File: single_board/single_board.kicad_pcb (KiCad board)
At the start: 4 copper layers, 100 x 100 mm, 121 parts, among them J11 SPI Debug, J17 BOOTSEL, J18 Power, J2 USB_C_Receptacle_USB2.0_16P, J3 SWD, J30 JST_GH_H, J31 JST_GH_H, J33 JST_GH_H, J34 PB_Vertical, J35 JST_GH_H, J36 JST_GH_H, J37 JST_GH_H, J38 PB_Vertical, J39 PB_Vertical, J40 PB_Vertical, J41 PB_Vertical, J42 PB_Vertical, J43 PB_Vertical, J44 PB_Vertical, J45 PB_Vertical, J46 PB_Vertical, J47 PB_Vertical, J48 PB_Vertical, J49 PB_Vertical, J5 JST-GH, J50 PB_Vertical, J53 PB_Vertical, Q1 AO3400A, Q3 AO3401A, SW1 Button, U1 AP2112K-3.3, U3 USBLC6-2SC6, U4 LSM6DSV, U5 STM32G474VBTx, Y2 ABM8-16MHz

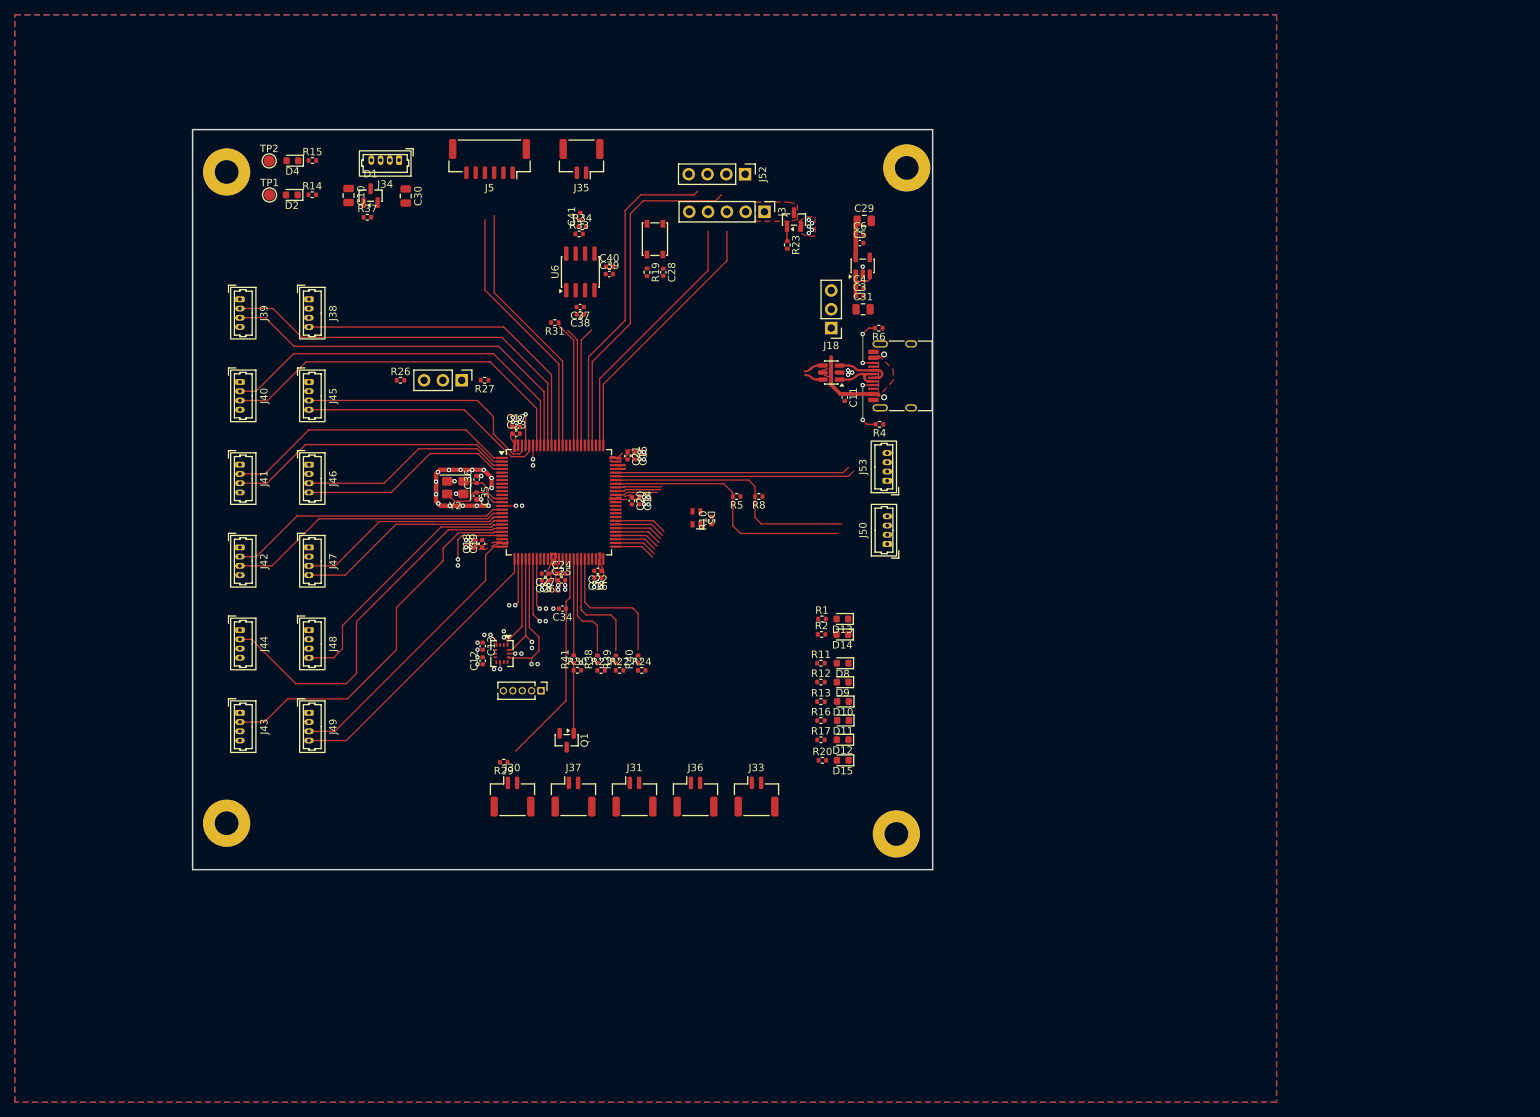
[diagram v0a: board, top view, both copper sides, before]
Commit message: Silkscreen on LEDs
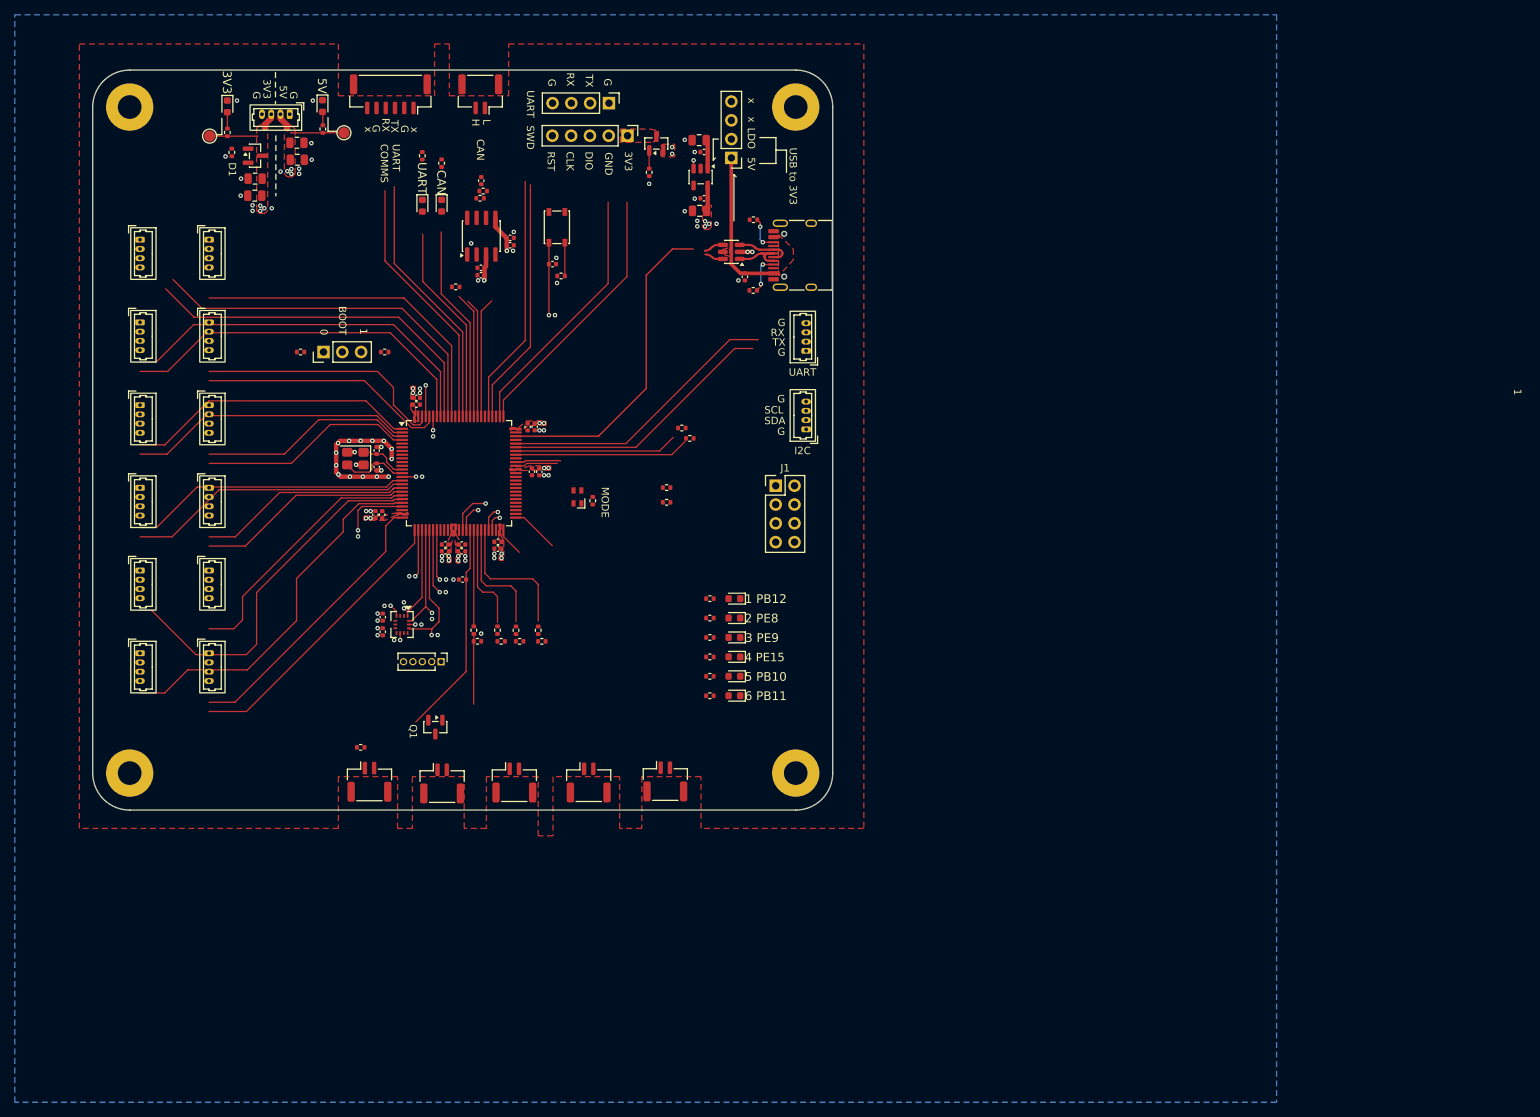
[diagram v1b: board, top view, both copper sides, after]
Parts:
- removed C4, C5: 100nF, Capacitor_SMD:C_0402_1005Metric
- removed J18: Power, Connector_PinHeader_2.54mm:PinHeader_1x03_P2.54mm_Vertical
- added C32: 22uF, Capacitor_SMD:C_0805_2012Metric, F.Cu at (73.5, 37.6)
- added C33: 22uF, Capacitor_SMD:C_0805_2012Metric, F.Cu at (67.8, 40.2)
- added J1: GPIO, Connector_PinHeader_2.54mm:PinHeader_2x04_P2.54mm_Vertical, F.Cu at (138.1, 81.7)
- added J56: Power, Connector_PinHeader_2.54mm:PinHeader_1x04_P2.54mm_Vertical, F.Cu at (132.1, 37.4)
- added R7: 5.1k, Resistor_SMD:R_0402_1005Metric, F.Cu at (123.4, 81.9)
- added R9: 5.1k, Resistor_SMD:R_0402_1005Metric, F.Cu at (123.4, 83.9)
- moved R2 84.2 mm to (90.3, 37.1), turned to 90 degrees
- moved D14 81.1 mm to (90.3, 43.9), turned to -90 degrees
- moved R1 80.2 mm to (93.0, 38.1), turned to 90 degrees
- moved D13 77.8 mm to (93.0, 43.9), turned to -90 degrees
- moved C31 31.8 mm to (127.8, 35.0), turned to 180 degrees
- moved C3 28.7 mm to (128.4, 36.6), turned to 180 degrees
- moved R27 25.2 mm to (73.9, 63.6), turned to 0 degrees
- moved U1 25.0 mm to (128.0, 40.0), turned to -90 degrees
- moved R4 24.9 mm to (135.1, 55.3), turned to 0 degrees
- moved R6 22.4 mm to (135.1, 45.8), turned to 0 degrees
- moved C29 22.3 mm to (127.8, 44.5), turned to 180 degrees
- moved C6 21.6 mm to (128.4, 42.9), turned to 180 degrees
- moved Q3 21.3 mm to (122.0, 35.5)
- moved J3 21.2 mm to (118.1, 34.4)
- moved U3 21.2 mm to (132.1, 50.1)
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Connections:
- D13 pad 1: GND -> Net-(D13-K)
- D13 pad 2: Net-(D13-A) -> /CAN_LED
- D14 pad 1: GND -> Net-(D14-K)
- D14 pad 2: Net-(D14-A) -> /UART_LED
- D2 pad 1: Net-(D2-K) -> GND
- D2 pad 2: 5V -> Net-(D2-A)
- D4 pad 1: Net-(D4-K) -> GND
- D4 pad 2: v3v3 -> Net-(D4-A)
- R1 pad 1: /CAN_LED -> Net-(D13-K)
- R1 pad 2: Net-(D13-A) -> GND
- R14 pad 1: Net-(D2-K) -> 5V
- R14 pad 2: GND -> Net-(D2-A)
- R15 pad 1: Net-(D4-K) -> v3v3
- R15 pad 2: GND -> Net-(D4-A)
- R2 pad 1: /HEARTBEAT -> Net-(D14-K)
- R2 pad 2: Net-(D14-A) -> GND
- U5 pad 39: unconnected-(U5-PE8-Pad39) -> /LED2
- U5 pad 40: unconnected-(U5-PE9-Pad40) -> /LED3
- U5 pad 46: unconnected-(U5-PE15-Pad46) -> /LED4
- U5 pad 47: unconnected-(U5-PB10-Pad47) -> /LED5
- U5 pad 50: unconnected-(U5-PB11-Pad50) -> /LED6
- U5 pad 51: /LED6 -> /LED1
- U5 pad 52: /LED5 -> /GPIO_8
- U5 pad 53: /LED4 -> /GPIO_7
- U5 pad 54: /LED3 -> /GPIO_6
- U5 pad 55: /LED2 -> /GPIO_5
- U5 pad 56: /LED1 -> /GPIO_4
- U5 pad 57: /HEARTBEAT -> /GPIO_3
- U5 pad 58: /CAN_LED -> unconnected-(U5-PD11-Pad58)
- U5 pad 59: unconnected-(U5-PD12-Pad59) -> /TRI_LED_G
- U5 pad 60: unconnected-(U5-PD13-Pad60) -> /TRI_LED_R
- U5 pad 61: unconnected-(U5-PD14-Pad61) -> /TRI_LED_B
- U5 pad 65: /TRI_LED_G -> /GPIO_1
- U5 pad 66: /TRI_LED_R -> /GPIO_2
- U5 pad 67: /TRI_LED_B -> unconnected-(U5-PC8-Pad67)
- U5 pad 85: unconnected-(U5-PD3-Pad85) -> /CAN_LED
- U5 pad 86: unconnected-(U5-PD4-Pad86) -> /UART_LED
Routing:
- net /USB-DP: track 3.87 -> 46.1 mm
- net /UART_LED: track 0.00 -> 27.1 mm
- net 5V: track 11.8 -> 35.6 mm, vias 0 -> 4
- net /CAN_LED: track 7.12 -> 26.5 mm
- net /I2C_SCL: track 35.5 -> 22.0 mm
- net /USART3_TX: track 46.9 -> 33.4 mm
- net v3v3: track 4.15 -> 17.4 mm, vias 16 -> 25
- net /I2C_SDA: track 35.4 -> 23.6 mm
- net /USART3_RX: track 44.7 -> 33.8 mm
- net /RST: track 1.89 -> 11.7 mm, vias 1 -> 2
- net /HEARTBEAT: track 6.94 -> 0.00 mm
- net /USART1_RX: track 31.8 -> 38.6 mm
- net /TRI_LED_B: track 6.26 -> 0.00 mm
- net /TRI_LED_R: track 6.11 -> 0.00 mm
- net /GPIO_2: track 0.00 -> 6.11 mm
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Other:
- outline, holes or cut-outs redrawn
- board text added: "0"
- board text added: "1"
- board text added: "1 PB12"
- board text added: "2 PE8"
- board text added: "3 PE9"
- board text added: "3V3"
- board text added: "4 PE15"
- board text added: "5 PB10"
- board text added: "5V"
- board text added: "6 PB11"
- board text added: "BOOT"
- board text added: "CAN"
- board text added: "CLK"
- board text added: "DIO"
- board text added: "FDCAN/CAN"
- board text added: "G"
- board text added: "GND"
- board text added: "H"
- board text added: "I2C"
- board text added: "I2C 3"
- board text added: "I2C 4"
- board text added: "L"
- board text added: "LDO"
- board text added: "MODE"
- board text added: "POWER"
- board text added: "RST"
- board text added: "RX"
- board text added: "SCL"
- board text added: "SDA"
- board text added: "SPI 2"
- board text added: "SWD"
- board text added: "TX"
- board text added: "UART"
- board text added: "UART COMMS"
- board text added: "UART1"
- board text added: "UART2"
- board text added: "UART3"
- board text added: "USB to 3V3"
- board text added: "x"

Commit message: UART Connector
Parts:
- removed J52: ~, Connector_PinHeader_2.54mm:PinHeader_1x04_P2.54mm_Vertical
- added J54: ~, rover:2.54 SMD, F.Cu at (108.1, 25.5)
- added J55: PB_Vertical, Connector_Molex:Molex_PicoBlade_53047-0410_1x04_P1.25mm_Vertical, F.Cu at (113.7, 30.5)
- moved J3 3.54 mm to (118.6, 37.9)
- moved Q3 3.54 mm to (122.5, 39.0)
- moved R23 3.54 mm to (121.6, 42.9)
- moved C28 0.98 mm to (108.9, 51.8)
- moved SW1 0.98 mm to (109.5, 46.9)
- moved R19 0.98 mm to (110.1, 53.4)
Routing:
- net /SWCLK: track 35.0 -> 24.0 mm
- net /SWDIO: track 35.9 -> 25.8 mm
- net /RST: track 11.7 -> 1.89 mm, vias 2 -> 1
- net Net-(R19-Pad1): track 4.50 -> 0.00 mm
- net GND: vias 79 -> 77

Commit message: GPIO
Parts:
- removed J1: GPIO, Connector_PinHeader_2.54mm:PinHeader_2x04_P2.54mm_Vertical
- added J57: PB_Vertical, Connector_Molex:Molex_PicoBlade_53047-0410_1x04_P1.25mm_Vertical, F.Cu at (142.2, 85.2)
- added J6: JST-GH, Connector_JST:JST_GH_SM06B-GHS-TB_1x06-1MP_P1.25mm_Horizontal, F.Cu at (140.8, 94.9)
- moved R2 9.70 mm to (90.3, 46.8)
- moved R1 8.70 mm to (93.0, 46.8)
- moved SW1 6.43 mm to (108.1, 53.1)
- moved J3 6.41 mm to (118.2, 44.3)
- moved Q3 6.41 mm to (122.1, 45.4)
- moved D10 5.94 mm to (127.7, 105.7)
- moved D11 5.94 mm to (127.7, 108.3)
- moved D12 5.94 mm to (127.7, 111.0)
- moved D15 5.94 mm to (127.7, 113.6)
- moved D8 5.94 mm to (127.7, 100.5)
- moved D9 5.94 mm to (127.7, 103.1)
- moved R11 5.94 mm to (124.4, 100.5)
- moved R12 5.94 mm to (124.4, 103.1)
- moved R13 5.94 mm to (124.4, 105.7)
- moved R16 5.94 mm to (124.4, 108.4)
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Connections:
- net /I2C_SCL renamed /I2C3_SCL
- net /I2C_SDA renamed /I2C3_SDA
- D13 pad 1: Net-(D13-K) -> GND
- D13 pad 2: /CAN_LED -> Net-(D13-A)
- D14 pad 1: Net-(D14-K) -> GND
- D14 pad 2: /UART_LED -> Net-(D14-A)
- R1 pad 1: Net-(D13-K) -> /CAN_LED
- R1 pad 2: GND -> Net-(D13-A)
- R2 pad 1: Net-(D14-K) -> /UART_LED
- R2 pad 2: GND -> Net-(D14-A)
- R7 pad 2: /GPIO_1 -> /I2C4_SDA
- R9 pad 2: /GPIO_2 -> /I2C4_SCL
- U5 pad 52: /GPIO_8 -> /SPI2_SCK
- U5 pad 53: /GPIO_7 -> /SPI2_MISO
- U5 pad 54: /GPIO_6 -> /SPI2_MOSI
- U5 pad 55: /GPIO_5 -> /SPI2_NSS
- U5 pad 56: /GPIO_4 -> unconnected-(U5-PD9-Pad56)
- U5 pad 57: /GPIO_3 -> unconnected-(U5-PD10-Pad57)
- U5 pad 65: /GPIO_1 -> /I2C4_SCL
- U5 pad 66: /GPIO_2 -> /I2C4_SDA
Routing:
- net /I2C4_SDA: track 0.00 -> 6.11 mm
- net /GPIO_2: track 6.11 -> 0.00 mm
- net /I2C4_SCL: track 0.00 -> 5.76 mm
- net /GPIO_1: track 5.76 -> 0.00 mm
- net Net-(Q3-G): track 2.46 -> 1.86 mm
- net GND: vias 77 -> 76
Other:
- board text added: "2"
- board text added: "3"
- board text added: "4"
- board text added: "5"
- board text added: "6"
- board text added: "PB10"
- board text added: "PB11"
- board text added: "PB12"
- board text added: "PE15"
- board text added: "PE8"
- board text added: "PE9"
- board text removed: "1 PB12"
- board text removed: "2 PE8"
- board text removed: "3 PE9"
- board text removed: "4 PE15"
- board text removed: "5 PB10"
- board text removed: "6 PB11"

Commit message: Arm Motor Silkscreen
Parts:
- moved H1 92.2 mm to (52.0, 122.7), turned to 90 degrees
- moved H2 91.3 mm to (142.1, 122.7), turned to 90 degrees
- moved H3 88.8 mm to (52.0, 32.7), turned to 90 degrees
- moved H4 87.8 mm to (142.1, 32.7), turned to 90 degrees
- moved D4 80.0 mm to (52.0, 109.5), turned to 0 degrees
- moved TP2 77.7 mm to (56.0, 111.9), turned to 0 degrees
- moved R15 76.0 mm to (55.5, 109.5), turned to 180 degrees
- moved J43 75.6 mm to (125.8, 121.3), turned to 0 degrees
- moved J39 75.0 mm to (70.0, 121.3), turned to 0 degrees
- moved J33 74.1 mm to (143.7, 50.5), turned to 90 degrees
- moved J56 73.3 mm to (58.9, 41.4), turned to -90 degrees
- moved J54 73.0 mm to (47.0, 65.5), turned to 90 degrees
- moved R37 72.5 mm to (58.2, 108.9), turned to 0 degrees
- moved J2 72.3 mm to (72.1, 31.7), turned to 180 degrees
- moved J34 72.3 mm to (53.0, 101.1), turned to -90 degrees
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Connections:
- J50 pad 2: /I2C3_SDA -> /I2C3_SCL
- J50 pad 3: /I2C3_SCL -> /I2C3_SDA
- J57 pad 2: /I2C4_SDA -> /I2C4_SCL
- J57 pad 3: /I2C4_SCL -> /I2C4_SDA
- R5 pad 2: /I2C3_SDA -> /I2C3_SCL
- R7 pad 2: /I2C4_SDA -> /I2C4_SCL
- R8 pad 2: /I2C3_SCL -> /I2C3_SDA
- R9 pad 2: /I2C4_SCL -> /I2C4_SDA
- U5 pad 67: unconnected-(U5-PC8-Pad67) -> /I2C3_SCL
- U5 pad 69: /I2C3_SCL -> unconnected-(U5-PA8-Pad69)
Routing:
- net /I2C3_SDA: track 23.6 -> 21.1 mm
- net /I2C3_SCL: track 22.0 -> 21.5 mm
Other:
- board text added: "A"
- board text added: "ABSOLUTE ENC"
- board text added: "B"
- board text added: "CONTROLS"
- board text added: "D"
- board text added: "DIR"
- board text added: "ENCODERS"
- board text added: "GPIO"
- board text added: "MISO"
- board text added: "MOSI"
- board text added: "NSS"
- board text added: "P"
- board text added: "PWM-IN"
- board text added: "PWM-OUT"
- board text added: "SCK"
- board text added: "SPI"
